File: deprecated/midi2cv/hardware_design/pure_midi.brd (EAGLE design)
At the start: 78.9 x 100 mm, 103 parts, among them IC1 STM32F373C, IC10 TL072CD, IC2 AD5754BREZ, IC4 TL072CD, IC5 6N138SMD, IC6 LD117AS33TR, IC7 TL072CD, IC8 ADR435, IC9 ADR431, J1 CORTEX_DEBUG_PTH, SW1 EC12E_SW, U2 AD5676ARUZ, X1 8MHz, X10 WQP-PJ301M-12_JACK, X11 WQP-PJ301M-12_JACK, X12 WQP-PJ301M-12_JACK, X13 WQP-PJ301M-12_JACK, X14 WQP-PJ301M-12_JACK, X15 WQP-PJ301M-12_JACK, X16 WQP-PJ301M-12_JACK, X17 WQP-PJ301M-12_JACK, X18 WQP-PJ301M-12_JACK, X19 WQP-PJ301M-12_JACK, X2 KUSBVX-BS1N, X20 WQP-PJ301M-12_JACK, X21 OG-MIDI_MAB5SHCUI-SD-50BV, X22 OG-MIDI_MAB5SHCUI-SD-50BV, X3 WQP-PJ301M-12_JACK, X4 WQP-PJ301M-12_JACK, X5 WQP-PJ301M-12_JACK, X6 WQP-PJ301M-12_JACK, X7 WQP-PJ301M-12_JACK, X8 WQP-PJ301M-12_JACK, X9 WQP-PJ301M-12_JACK

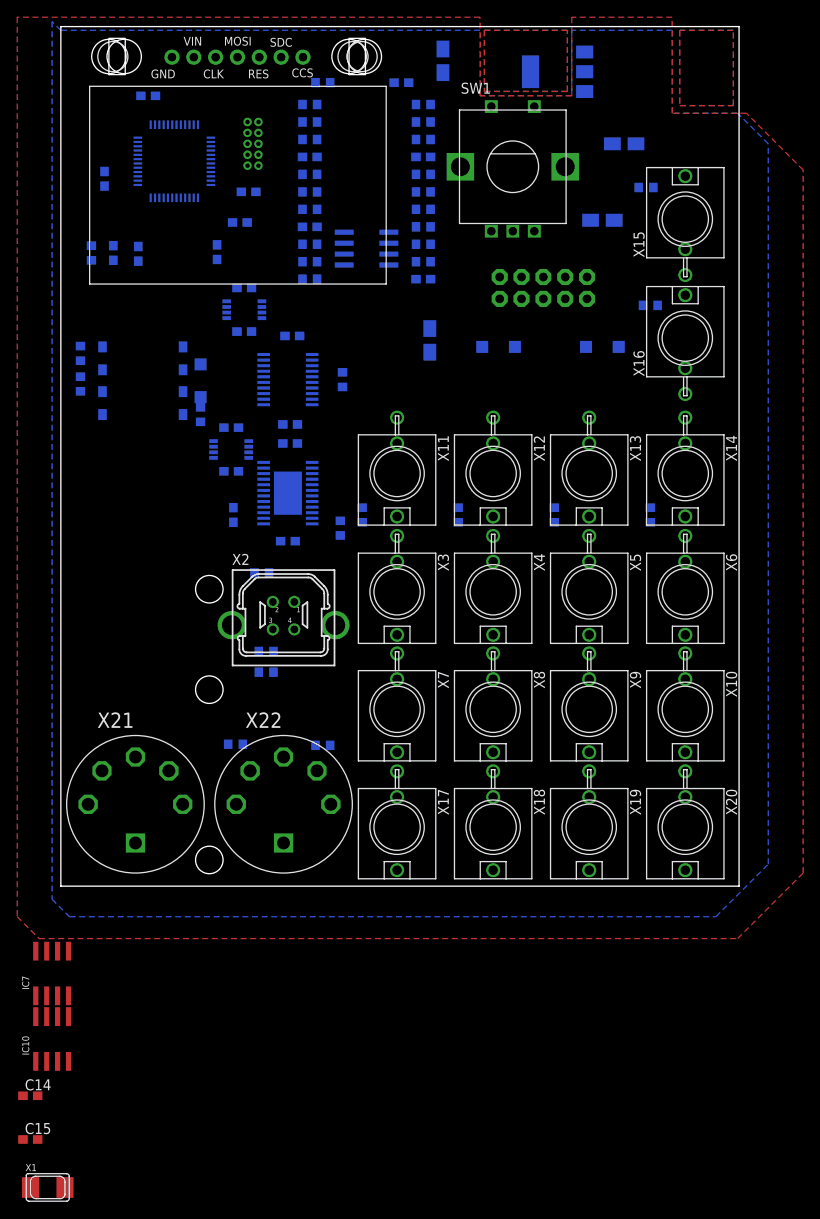
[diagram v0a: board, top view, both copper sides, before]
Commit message: Move midi2cv to deprecated folder
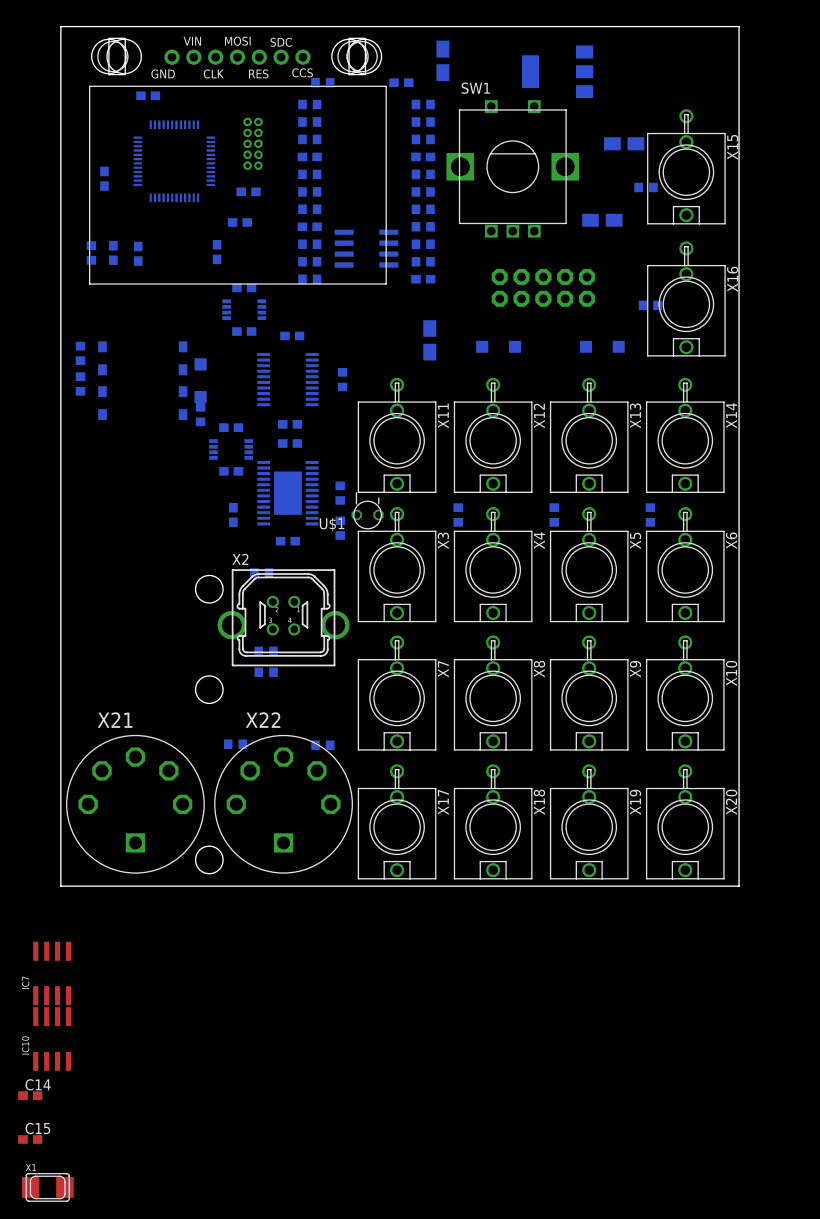
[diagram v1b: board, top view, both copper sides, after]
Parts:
- added U$1: LED-BICOLOR-SHARED-THROUGHHOLE, jhbruhn-physical:LED3MM
- moved X15 5.46 mm to (72.8, 83.1), turned to 180 degrees
- moved X16 3.94 mm to (72.8, 67.7), turned to 180 degrees
- moved X11 3.81 mm to (39.1, 51.8)
- moved X12 3.81 mm to (50.3, 51.8)
- moved X13 3.81 mm to (61.5, 51.8)
- moved X14 3.81 mm to (72.6, 51.8)
- moved R10 3.59 mm to (32.5, 45.7)
- moved X3 2.54 mm to (39.1, 36.8)
- moved X4 2.54 mm to (50.3, 36.8)
- moved X5 2.54 mm to (61.5, 36.8)
- moved X6 2.54 mm to (72.6, 36.8)
- moved X10 1.27 mm to (72.6, 21.8)
- moved X7 1.27 mm to (39.1, 21.8)
- moved X8 1.27 mm to (50.3, 21.8)
- moved X9 1.27 mm to (61.5, 21.8)
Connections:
- removed net RST_USB: IC1.42
- removed net SS_USB: IC1.43
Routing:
- removed copper zone on layer 1, net +3V3
- removed copper zone on layer 16, net +3V3
- removed copper zone on layer 1, net +5V
- removed copper zone on layer 16, net +5V
- removed copper zone on layer 1, net GND
- removed copper zone on layer 16, net GND
